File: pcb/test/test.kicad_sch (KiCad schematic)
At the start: 2 parts, among them IC1 ADG904BRUZ-REEL7

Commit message: first schematic
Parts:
- added ANT2, ANT3: ST0147-00-011-A, ANTC3016X55N, symbol test_library:ST0147-00-011-A
- added J1: MM8130-2600RA2, MM8130-2600RA2:MURATA_MM8130-2600RA2, symbol test_library:MM8130-2600RA2
- added J3: Conn_01x04, symbol Connector_Generic:Conn_01x04
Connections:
- net GND: now reaches IC1.1 (~{EN})
- net GND: now also ANT1.2 (NC), IC1.3 (GND_1), ANT2.2 (NC), ANT3.2 (NC), J1.GND1 (GND), J1.GND2 (GND), J1.GND3 (GND), J1.GND4 (GND), J3.1 (Pin_1)
- net at IC1.10 (RFC): now also J1.OUT
- net at IC1.17 (RF2): now also ANT2.1 (FEED)
- net at IC1.19 (A1): now also J3.3 (Pin_3)
- net +2V5: now reaches IC1.2 (VDD)
- net at IC1.20 (A0): now also J3.2 (Pin_2)
- net at IC1.4 (RF1): now also ANT1.1 (FEED)
- net at IC1.7 (RF3): now also ANT3.1 (FEED)
- new net +5V: J3.4 (Pin_4)
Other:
- moved on the sheet: ANT1

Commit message: j'ai oublié ce que j'ai fait
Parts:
- removed J1: MM8130-2600RA2, MM8130-2600RA2:MURATA_MM8130-2600RA2, symbol test_library:MM8130-2600RA2
- added J1: CONSMA013.062-G, CONSMA013.062-G:LINX_CONSMA013.062-G, symbol test_library:CONSMA013.062-G
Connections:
- net GND: now also J1.S1, J1.S2, J1.S3, J1.S4
- net at IC1.10 (RFC): now also J1.1
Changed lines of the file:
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@@
 	(wire
 		(pts
-			(xy 59.69 177.8) (xy 49.53 177.8)
+			(xy 33.02 177.8) (xy 59.69 177.8)
 		)
 		(stroke
@@
 	(wire
 		(pts
-			(xy 60.96 172.72) (xy 49.53 172.72)
-		)
-		(stroke
-			(width 0)
-			(type default)
-		)
-	)
-	(wire
-		(pts
 			(xy 59.69 184.15) (xy 59.69 177.8)
 		)
@@
 	(wire
 		(pts
+			(xy 33.02 175.26) (xy 60.96 175.26)
+		)
+		(stroke
+			(width 0)
+			(type default)
+		)
+	)
+	(wire
+		(pts
 			(xy 107.95 130.81) (xy 35.56 130.81)
 		)
@@
 	(wire
 		(pts
-			(xy 60.96 146.05) (xy 60.96 172.72)
+			(xy 60.96 146.05) (xy 60.96 175.26)
 		)
 		(stroke
@@
 			(width 0)
 			(type default)
-		)
-	)
-	(symbol
-		(lib_id "test_library:MM8130-2600RA2")
-		(at 39.37 175.26 0)
-		(unit 1)
-		(exclude_from_sim no)
-		(in_bom yes)
-		(on_board yes)
-		(dnp no)
-		(fields_autoplaced yes)
-		(property "Reference" "J1"
-			(at 39.37 165.1 0)
-			(effects
-				(font
-					(size 1.27 1.27)
-				)
-			)
-		)
-		(property "Value" "MM8130-2600RA2"
-			(at 39.37 167.64 0)
-			(effects
-				(font
-					(size 1.27 1.27)
-				)
-			)
-		)
-		(property "Footprint" "MM8130-2600RA2:MURATA_MM8130-2600RA2"
-			(at 39.37 175.26 0)
-			(effects
-				(font
-					(size 1.27 1.27)
-				)
-				(justify bottom)
-				(hide yes)
-			)
-		)
-		(property "Datasheet" ""
-			(at 39.37 175.26 0)
-			(effects
-				(font
-					(size 1.27 1.27)
-				)
-				(hide yes)
-			)
-		)
-		(property "Description" ""
-			(at 39.37 175.26 0)
-			(effects
-				(font
-					(size 1.27 1.27)
-				)
-				(hide yes)
-			)
-		)
-		(property "MF" "Murata"
-			(at 39.37 175.26 0)
-			(effects
-				(font
-					(size 1.27 1.27)
-				)
-				(justify bottom)
-				(hide yes)
-			)
-		)
-		(property "Description_1" "\n                        \n                            SWF Connector Receptacle, Female Socket 50 Ohms Surface Mount Solder\n                        \n"
-			(at 39.37 175.26 0)
-			(effects
-				(font
-					(size 1.27 1.27)
-				)
-				(justify bottom)
-				(hide yes)
-			)
-		)
-		(property "Package" "None"
-			(at 39.37 175.26 0)
-			(effects
-				(font
-					(size 1.27 1.27)
-				)
-				(justify bottom)
-				(hide yes)
-			)
-		)
-		(property "Price" "None"
-			(at 39.37 175.26 0)
-			(effects
-				(font
-					(size 1.27 1.27)
-				)
-				(justify bottom)
-				(hide yes)
-			)
-		)
-		(property "Check_prices" "https://www.snapeda.com/parts/MM8130-2600RA2/Murata/view-part/?ref=eda"
-			(at 39.37 175.26 0)
-			(effects
-				(font
-					(size 1.27 1.27)
-				)
-				(justify bottom)
-				(hide yes)
-			)
-		)
-		(property "SnapEDA_Link" "https://www.snapeda.com/parts/MM8130-2600RA2/Murata/view-part/?ref=snap"
-			(at 39.37 175.26 0)
-			(effects
-				(font
-					(size 1.27 1.27)
-				)
-				(justify bottom)
-				(hide yes)
-			)
-		)
-		(property "MP" "MM8130-2600RA2"
-			(at 39.37 175.26 0)
-			(effects
-				(font
-					(size 1.27 1.27)
-				)
-				(justify bottom)
-				(hide yes)
-			)
-		)
-		(property "Availability" "In Stock"
-			(at 39.37 175.26 0)
-			(effects
-				(font
-					(size 1.27 1.27)
-				)
-				(justify bottom)
-				(hide yes)
-			)
-		)
-		(property "MANUFACTURER" "MURATA"
-			(at 39.37 175.26 0)
-			(effects
-				(font
-					(size 1.27 1.27)
-				)
-				(justify bottom)
-				(hide yes)
-			)
-		)
-		(pin "GND3"
-		)
-		(pin "GND2"
-		)
-		(pin "IN"
-		)
-		(pin "GND4"
-		)
-		(pin "OUT"
-		)
-		(pin "GND1"
-		)
-		(instances
-			(project ""
-				(path "/bb1015a8-5dcf-444f-b1dc-3665f721c6b4"
-					(reference "J1")
-					(unit 1)
-				)
-			)
 		)
 	)
@@
 					(unit 1)
 				)
+			)
+		)
+	)
+	(symbol
+		(lib_id "test_library:CONSMA013.062-G")
+		(at 30.48 175.26 0)
+		(mirror y)
+		(unit 1)
+		(exclude_from_sim no)
+		(in_bom yes)
+		(on_board yes)
+		(dnp no)
+		(fields_autoplaced yes)
+		(property "Reference" "J1"
+			(at 29.4072 168.91 0)
+			(effects
+				(font
+					(size 1.27 1.27)
+				)
+			)
+		)
+		(property "Value" "CONSMA013.062-G"
+			(at 29.4072 171.45 0)
+			(effects
+				(font
+					(size 1.27 1.27)
+				)
+			)
+		)
+		(property "Footprint" "CONSMA013.062-G:LINX_CONSMA013.062-G"
+			(at 30.48 175.26 0)
+			(effects
+				(font
+					(size 1.27 1.27)
+				)
+				(justify bottom)
+				(hide yes)
+			)
+		)
+		(property "Datasheet" ""
+			(at 30.48 175.26 0)
+			(effects
+				(font
+					(size 1.27 1.27)
+				)
+				(hide yes)
+			)
+		)
+		(property "Description" ""
+			(at 30.48 175.26 0)
+			(effects
+				(font
+					(size 1.27 1.27)
+				)
+				(hide yes)
+			)
+		)
+		(property "MF" "Linx Technologies"
+			(at 30.48 175.26 0)
+			(effects
+				(font
+					(size 1.27 1.27)
+				)
+				(justify bottom)
+				(hide yes)
+			)
+		)
+		(property "MAXIMUM_PACKAGE_HEIGHT" "4.3mm"
+			(at 30.48 175.26 0)
+			(effects
+				(font
+					(size 1.27 1.27)
+				)
+				(justify bottom)
+				(hide yes)
+			)
+		)
+		(property "Package" "None"
+			(at 30.48 175.26 0)
+			(effects
+				(font
+					(size 1.27 1.27)
+				)
+				(justify bottom)
+				(hide yes)
+			)
+		)
+		(property "Price" "None"
+			(at 30.48 175.26 0)
+			(effects
+				(font
+					(size 1.27 1.27)
+				)
+				(justify bottom)
+				(hide yes)
+			)
+		)
+		(property "Check_prices" "https://www.snapeda.com/parts/CONSMA013.062-G/Linx/view-part/?ref=eda"
+			(at 30.48 175.26 0)
+			(effects
+				(font
+					(size 1.27 1.27)
+				)
+				(justify bottom)
+				(hide yes)
+			)
+		)
+		(property "STANDARD" "Manufacturer Recommendations"
+			(at 30.48 175.26 0)
+			(effects
+				(font
+					(size 1.27 1.27)
+				)
+				(justify bottom)
+				(hide yes)
+			)
+		)
+		(property "PARTREV" "A"
+			(at 30.48 175.26 0)
+			(effects
+				(font
+					(size 1.27 1.27)
+				)
+				(justify bottom)
+				(hide yes)
+			)
+		)
+		(property "SnapEDA_Link" "https://www.snapeda.com/parts/CONSMA013.062-G/Linx/view-part/?ref=snap"
+			(at 30.48 175.26 0)
+			(effects
+				(font
+					(size 1.27 1.27)
+				)
+				(justify bottom)
+				(hide yes)
+			)
+		)
+		(property "MP" "CONSMA013.062-G"
+			(at 30.48 175.26 0)
+			(effects
+				(font
+					(size 1.27 1.27)
+				)
+				(justify bottom)
+				(hide yes)
+			)
+		)
+		(property "Description_1" "\n                        \n                            SMA Plug 50 Ohm .062 PCB Edge Mount\n                        \n"
+			(at 30.48 175.26 0)
+			(effects
+				(font
+					(size 1.27 1.27)
+				)
+				(justify bottom)
+				(hide yes)
+			)
+		)
+		(property "Availability" "In Stock"
+			(at 30.48 175.26 0)
+			(effects
+				(font
+					(size 1.27 1.27)
+				)
+				(justify bottom)
+				(hide yes)
+			)
+		)
+		(property "MANUFACTURER" "Linx Technologies"
+			(at 30.48 175.26 0)
+			(effects
+				(font
+					(size 1.27 1.27)
+				)
+				(justify bottom)
+				(hide yes)
+			)
+		)
+		(pin "1"
+		)
+		(pin "S2"
+		)
+		(pin "S1"
+		)
+		(pin "S3"
+		)
+		(pin "S4"
+		)
+		(instances
+			(project ""
+				(path "/bb1015a8-5dcf-444f-b1dc-3665f721c6b4"
+					(reference "J1")
+					(unit 1)
+				)

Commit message: schematic finished ?
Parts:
- added C1, C3: C, symbol Device:C
- added C2: C_Polarized, symbol Device:C_Polarized
- added R1, R2: R, symbol Device:R
- added U1: MCP601R, Package_TO_SOT_SMD:SOT-23-5, symbol Amplifier_Operational:MCP601R
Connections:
- net +2V5: now also C3.1, U1.1, U1.4 (-)
- net +5V: now also C1.1, C2.1, R1.1, U1.2 (V+)
- net GND: now also IC1.11 (GND_6), C1.2, C2.2, C3.2, R2.2, U1.5 (V-); no longer IC1.3 (GND_1)
- new net: R1.2, R2.1, U1.3 (+)

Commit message: empreintes
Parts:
- C1, C2, C3: footprint (none) -> Capacitor_SMD:CP_Elec_6.3x5.4
- J1: footprint CONSMA013.062-G:LINX_CONSMA013.062-G -> test_footprint_library:LINX_CONSMA013.062-G
- J3: footprint (none) -> Connector_PinHeader_2.54mm:PinHeader_1x04_P2.54mm_Horizontal
- R1, R2: footprint (none) -> Resistor_THT:R_Axial_DIN0411_L9.9mm_D3.6mm_P15.24mm_Horizontal
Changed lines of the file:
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@@
 			)
 		)
-		(property "Footprint" ""
+		(property "Footprint" "Capacitor_SMD:CP_Elec_6.3x5.4"
 			(at 112.7252 181.61 0)
 			(effects
@@
 					(size 1.27 1.27)
 				)
-				(hide yes)
 			)
 		)
@@
 			)
 		)
-		(property "Footprint" ""
+		(property "Footprint" "Resistor_THT:R_Axial_DIN0411_L9.9mm_D3.6mm_P15.24mm_Horizontal"
 			(at 219.202 137.16 90)
 			(effects
@@
 					(size 1.27 1.27)
 				)
-				(hide yes)
 			)
 		)
@@
 			)
 		)
-		(property "Footprint" "CONSMA013.062-G:LINX_CONSMA013.062-G"
+		(property "Footprint" "test_footprint_library:LINX_CONSMA013.062-G"
 			(at 30.48 175.26 0)
 			(effects
@@
 				)
 				(justify bottom)
-				(hide yes)
 			)
 		)
@@
 			)
 		)
-		(property "Footprint" ""
+		(property "Footprint" "Connector_PinHeader_2.54mm:PinHeader_1x04_P2.54mm_Horizontal"
 			(at 19.05 115.57 0)
 			(effects
@@
 					(size 1.27 1.27)
 				)
-				(hide yes)
 			)
 		)
@@
 			)
 		)
-		(property "Footprint" ""
+		(property "Footprint" "Capacitor_SMD:CP_Elec_6.3x5.4"
 			(at 257.5052 142.24 0)
 			(effects
@@
 					(size 1.27 1.27)
 				)
-				(hide yes)
 			)
 		)
@@
 			)
 		)
-		(property "Footprint" ""
+		(property "Footprint" "Capacitor_SMD:CP_Elec_6.3x5.4"
 			(at 100.0252 181.61 0)
 			(effects
@@
 					(size 1.27 1.27)
 				)
-				(hide yes)
 			)
 		)
@@
 			)
 		)
-		(property "Footprint" ""
+		(property "Footprint" "Resistor_THT:R_Axial_DIN0411_L9.9mm_D3.6mm_P15.24mm_Horizontal"
 			(at 219.202 127 90)
 			(effects
@@
 					(size 1.27 1.27)
 				)
-				(hide yes)
-			)
-		)
+			)
+		)

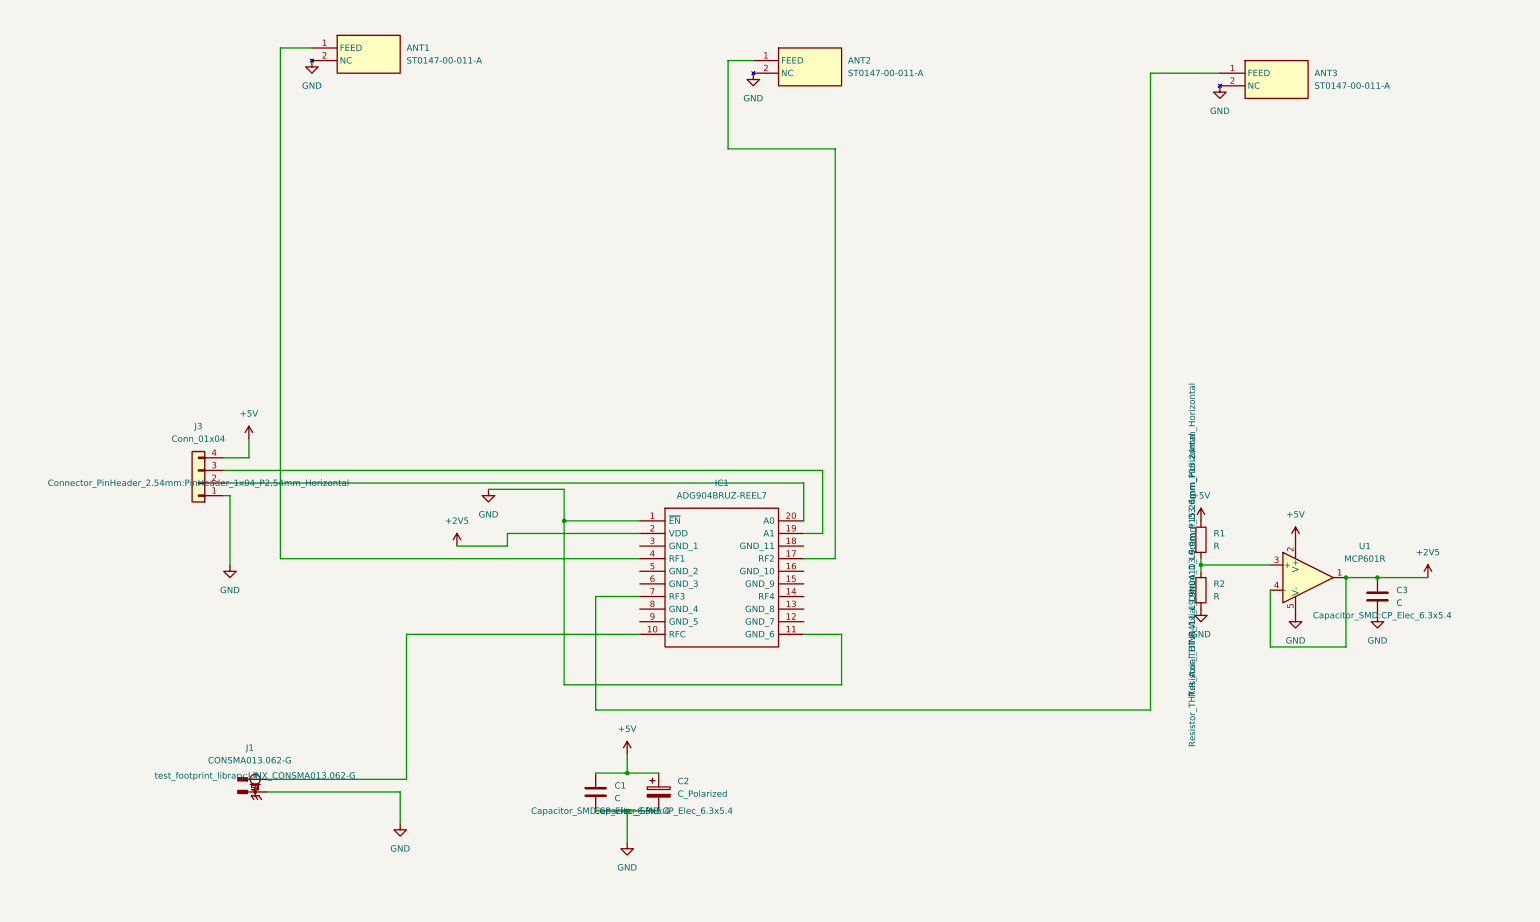
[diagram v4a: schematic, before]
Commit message: composants placés sur pcb
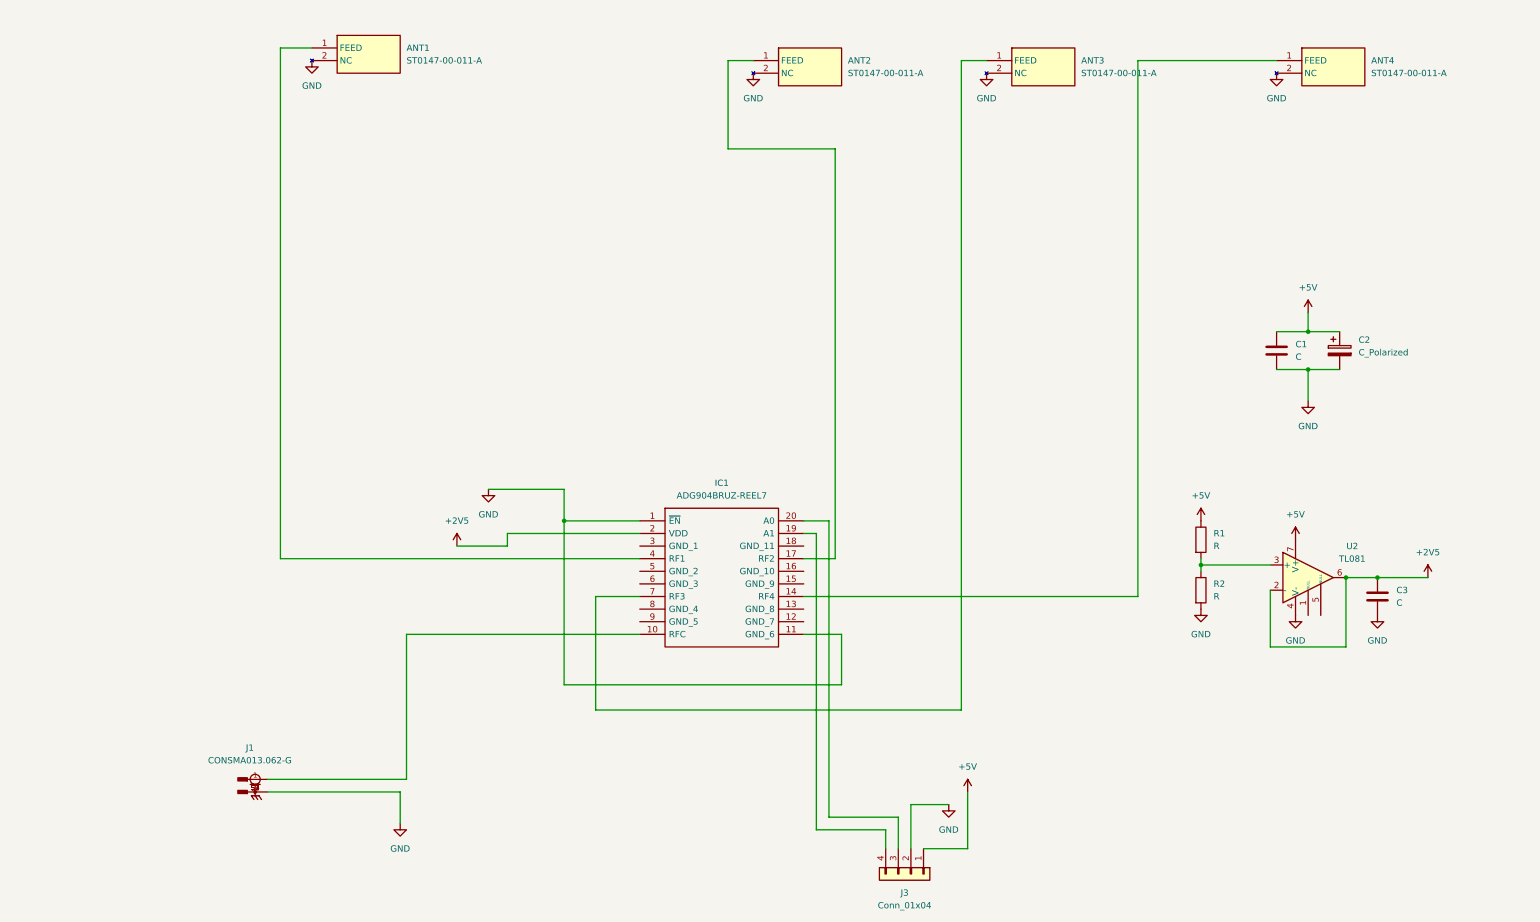
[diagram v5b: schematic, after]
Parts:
- removed U1: MCP601R, Package_TO_SOT_SMD:SOT-23-5, symbol Amplifier_Operational:MCP601R
- added ANT4: ST0147-00-011-A, ANTC3016X55N, symbol test_library:ST0147-00-011-A
- added U2: TL081, Package_DIP:DIP-8_W7.62mm, symbol Amplifier_Operational:TL081
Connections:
- net +2V5: now also U2.2 (-), U2.6
- net +5V: now also J3.1 (Pin_1), U2.7 (V+); no longer J3.4 (Pin_4)
- net GND: now also J3.2 (Pin_2), ANT4.2 (NC), U2.4 (V-); no longer J3.1 (Pin_1)
- net at R1.2, R2.1: now also U2.3 (+)
- net at IC1.20 (A0): now also J3.3 (Pin_3); no longer J3.2 (Pin_2)
- net at IC1.19 (A1): now also J3.4 (Pin_4); no longer J3.3 (Pin_3)
- net at IC1.14 (RF4): now also ANT4.1 (FEED)
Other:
- moved on the sheet: ANT3, C1, C2, J3

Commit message: pistes
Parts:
- added JP1, JP2: Jumper_2_Bridged, test_footprint_library:jumper20, symbol Jumper:Jumper_2_Bridged
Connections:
- net at IC1.20 (A0): now also JP2.1 (A); no longer J3.3 (Pin_3)
- net at IC1.19 (A1): now also JP1.1 (A); no longer J3.4 (Pin_4)
- new net: J3.3 (Pin_3), JP2.2 (B)
- new net: J3.4 (Pin_4), JP1.2 (B)
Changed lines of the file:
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@@
+	(wire
+		(pts
+			(xy 148.59 182.88) (xy 146.05 182.88)
+		)
+		(stroke
+			(width 0)
+			(type default)
+		)
+	)
 	(wire
 		(pts
@@
 	(wire
 		(pts
-			(xy 160.02 182.88) (xy 146.05 182.88)
+			(xy 160.02 182.88) (xy 158.75 182.88)
 		)
 		(stroke
@@
 	(wire
 		(pts
+			(xy 41.91 30.48) (xy 41.91 34.29)
+		)
+		(stroke
+			(width 0)
+			(type default)
+		)
+	)
+	(wire
+		(pts
 			(xy 107.95 138.43) (xy 99.06 138.43)
 		)
@@
 	(wire
 		(pts
-			(xy 157.48 185.42) (xy 143.51 185.42)
+			(xy 157.48 185.42) (xy 154.94 185.42)
 		)
 		(stroke
@@
 		(pts
 			(xy 248.92 85.09) (xy 242.57 85.09)
+		)
+		(stroke
+			(width 0)
+			(type default)
+		)
+	)
+	(wire
+		(pts
+			(xy 144.78 185.42) (xy 143.51 185.42)
 		)
 		(stroke
@@
 	)
 	(symbol
+		(lib_id "Jumper:Jumper_2_Bridged")
+		(at 153.67 182.88 0)
+		(unit 1)
+		(exclude_from_sim yes)
+		(in_bom yes)
+		(on_board yes)
+		(dnp no)
+		(fields_autoplaced yes)
+		(property "Reference" "JP2"
+			(at 153.67 177.8 0)
+			(effects
+				(font
+					(size 1.27 1.27)
+				)
+			)
+		)
+		(property "Value" "Jumper_2_Bridged"
+			(at 153.67 180.34 0)
+			(effects
+				(font
+					(size 1.27 1.27)
+				)
+				(hide yes)
+			)
+		)
+		(property "Footprint" "test_footprint_library:jumper20"
+			(at 153.67 182.88 0)
+			(effects
+				(font
+					(size 1.27 1.27)
+				)
+				(hide yes)
+			)
+		)
+		(property "Datasheet" "~"
+			(at 153.67 182.88 0)
+			(effects
+				(font
+					(size 1.27 1.27)
+				)
+				(hide yes)
+			)
+		)
+		(property "Description" "Jumper, 2-pole, closed/bridged"
+			(at 153.67 182.88 0)
+			(effects
+				(font
+					(size 1.27 1.27)
+				)
+				(hide yes)
+			)
+		)
+		(pin "2"
+		)
+		(pin "1"
+		)
+		(instances
+			(project "test"
+				(path "/bb1015a8-5dcf-444f-b1dc-3665f721c6b4"
+					(reference "JP2")
+					(unit 1)
+				)
+			)
+		)
+	)
+	(symbol
 		(lib_id "power:GND")
 		(at 177.8 33.02 0)
@@
 				(path "/bb1015a8-5dcf-444f-b1dc-3665f721c6b4"
 					(reference "ANT4")
+					(unit 1)
+				)
+			)
+		)
+	)
+	(symbol
+		(lib_id "Jumper:Jumper_2_Bridged")
+		(at 149.86 185.42 0)
+		(unit 1)
+		(exclude_from_sim yes)
+		(in_bom yes)
+		(on_board yes)
+		(dnp no)
+		(fields_autoplaced yes)
+		(property "Reference" "JP1"
+			(at 149.86 180.34 0)
+			(effects
+				(font
+					(size 1.27 1.27)
+				)
+			)
+		)
+		(property "Value" "Jumper_2_Bridged"
+			(at 149.86 182.88 0)
+			(effects
+				(font
+					(size 1.27 1.27)
+				)
+				(hide yes)
+			)
+		)
+		(property "Footprint" "test_footprint_library:jumper20"
+			(at 149.86 185.42 0)
+			(effects
+				(font
+					(size 1.27 1.27)
+				)
+				(hide yes)
+			)
+		)
+		(property "Datasheet" "~"
+			(at 149.86 185.42 0)
+			(effects
+				(font
+					(size 1.27 1.27)
+				)
+				(hide yes)
+			)
+		)
+		(property "Description" "Jumper, 2-pole, closed/bridged"
+			(at 149.86 185.42 0)
+			(effects
+				(font
+					(size 1.27 1.27)
+				)
+				(hide yes)
+			)
+		)
+		(pin "2"
+		)
+		(pin "1"
+		)
+		(instances
+			(project ""
+				(path "/bb1015a8-5dcf-444f-b1dc-3665f721c6b4"
+					(reference "JP1")
 					(unit 1)
 				)
@@
 	(symbol
 		(lib_id "power:GND")
-		(at 41.91 30.48 0)
+		(at 41.91 34.29 0)
 		(unit 1)
 		(exclude_from_sim no)
@@
 		(fields_autoplaced yes)
 		(property "Reference" "#PWR04"
-			(at 41.91 36.83 0)
+			(at 41.91 40.64 0)
 			(effects
 				(font
@@
 		)
 		(property "Value" "GND"
-			(at 41.91 35.56 0)
+			(at 41.91 39.37 0)
 			(effects
 				(font
@@
 		)
 		(property "Footprint" ""
-			(at 41.91 30.48 0)
+			(at 41.91 34.29 0)
 			(effects
 				(font
@@
 		)
 		(property "Datasheet" ""
-			(at 41.91 30.48 0)
+			(at 41.91 34.29 0)
 			(effects
 				(font
@@
 		)
 		(property "Description" "Power symbol creates a global label with name \"GND\" , ground"
-			(at 41.91 30.48 0)
-			(effects
-				(font
+			(at 41.91 34.29 0)
+			(effects
+				(font

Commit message: séance 18/12
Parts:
- added C4: C, symbol Device:C
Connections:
- net GND: now also IC1.12 (GND_7), IC1.13 (GND_8), IC1.15 (GND_9), IC1.16 (GND_10), IC1.18 (GND_11), IC1.3 (GND_1), IC1.5 (GND_2), IC1.6 (GND_3), IC1.8 (GND_4), IC1.9 (GND_5)
- net at IC1.4 (RF1): no longer ANT1.1 (FEED)
